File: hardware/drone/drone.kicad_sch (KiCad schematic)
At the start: 0 parts

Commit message: save before nuke
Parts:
- added H101: MountingHole, MountingHole:MountingHole_2.2mm_M2_DIN965, symbol Mechanical:MountingHole
- added H102, H103, H104, H105: MountingHole_Pad, SamacSys_Parts:MountingHole_4.3mm_M4_ISO14580_Pad, symbol Mechanical:MountingHole_Pad
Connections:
- new net GND: H102.1, H103.1, H104.1, H105.1
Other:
- added sheet ESP32 (ESP32.kicad_sch)
- added sheet LEDS (LEDS.kicad_sch)
- added sheet LOCALIZATION (IMU.kicad_sch)
- added sheet MOTORS (MOTORS.kicad_sch)
- added sheet POWER (POWER.kicad_sch)
- added sheet USBC (USBC.kicad_sch)
- note added: "Mounting Holes"
- title: (none) -> Remote Controller

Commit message: save before axing motor driver ic's
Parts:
- removed H101: MountingHole, MountingHole:MountingHole_2.2mm_M2_DIN965, symbol Mechanical:MountingHole
- renumbered H102 to H2, H103 to H3, H104 to H4, H105 to H5
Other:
- sheet ESP32 ports: added BARO.CS, BARO.INT, D+, D-, IMU.INT1, IMU.INT2, IMU_CS, MD{MOTOR_DRIVER}, SPI{SPI}; removed LED_GPIO, USB+, USB-
- sheet LEDS ports: added none; removed LED_GPIO
- sheet LOCALIZATION ports: added BARO.CS, BARO.INT, IMU.INT1, IMU.INT2, IMU_CS, SPI{SPI}; removed none
- sheet MOTORS ports: added MD{MOTOR_DRIVER}; removed none
- sheet USBC ports: added D+, D-; removed USB+, USB-

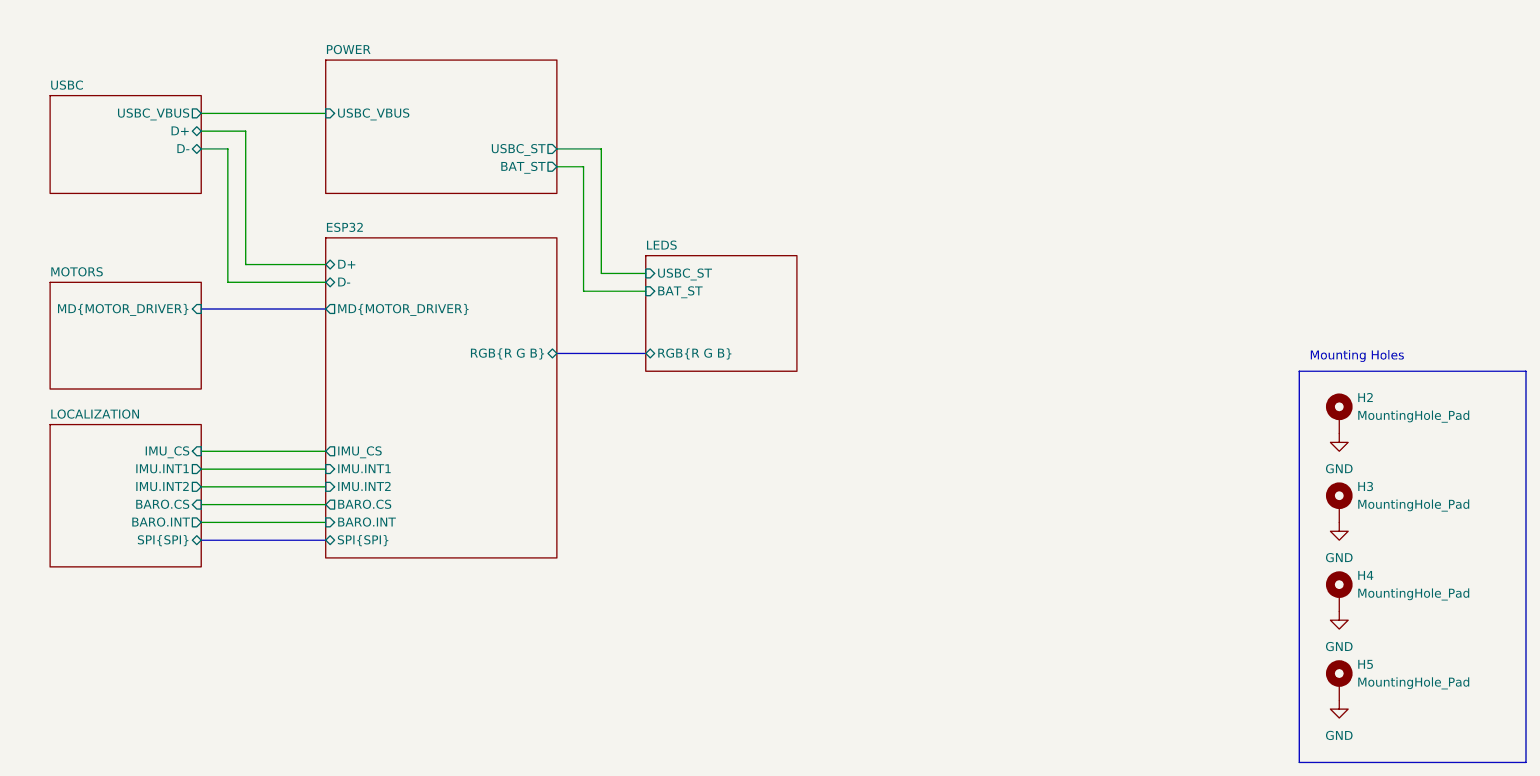
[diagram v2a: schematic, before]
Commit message: axed motor drivers. finished layout for drone but need to review overall system design after reading some stuff
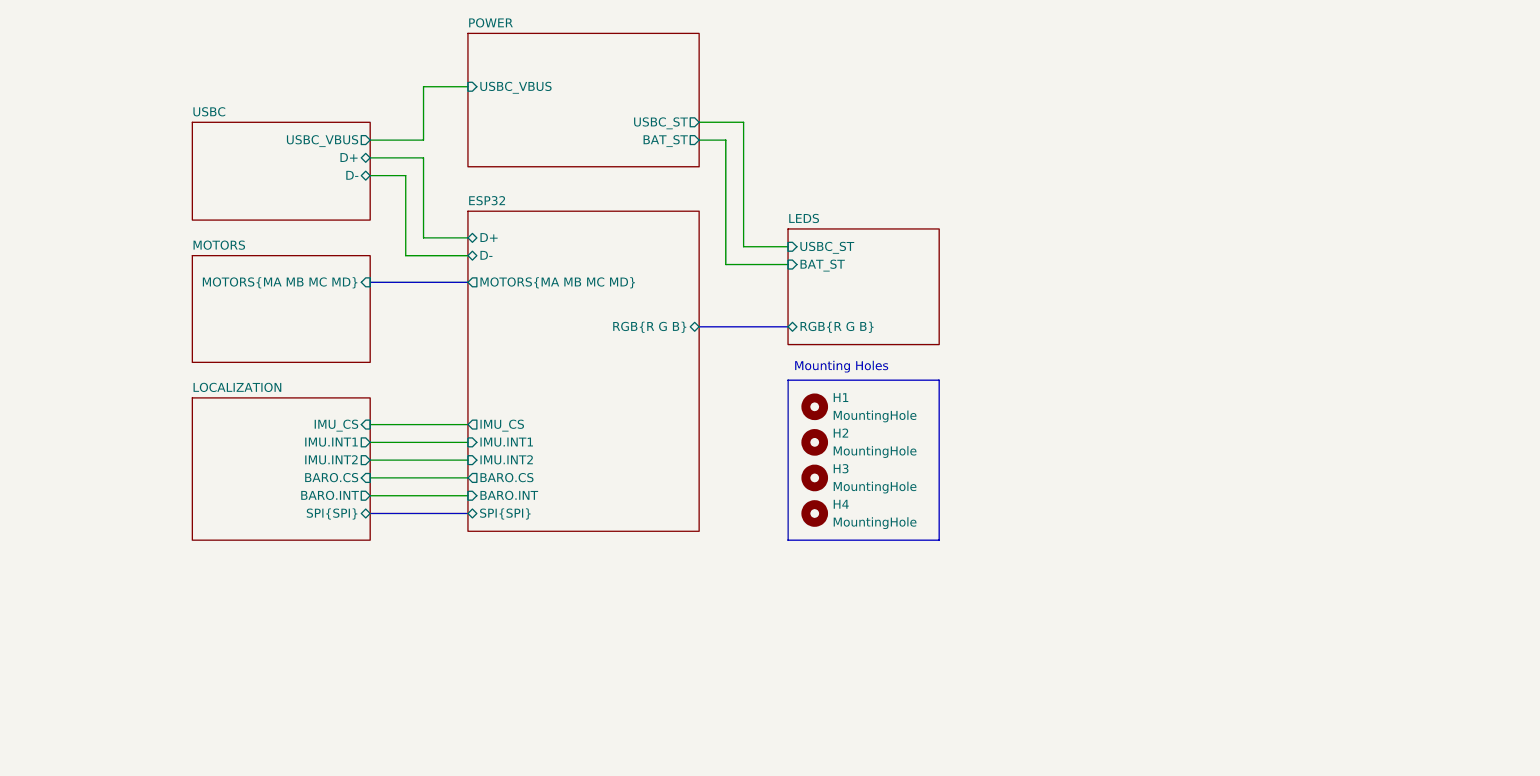
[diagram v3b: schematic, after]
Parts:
- removed H2, H3, H4, H5: MountingHole_Pad, SamacSys_Parts:MountingHole_4.3mm_M4_ISO14580_Pad, symbol Mechanical:MountingHole_Pad
- added H1, H2, H3, H4: MountingHole, MountingHole:MountingHole_2.1mm, symbol Mechanical:MountingHole
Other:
- sheet ESP32 ports: added MOTORS{MA MB MC MD}; removed MD{MOTOR_DRIVER}
- sheet MOTORS ports: added MOTORS{MA MB MC MD}; removed MD{MOTOR_DRIVER}
